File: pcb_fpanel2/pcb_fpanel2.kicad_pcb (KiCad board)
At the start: 2 copper layers, 155.5 x 65.5 mm, 22 parts, among them J1 Conn_01x10, SW1 SW_Push_LED, SW2 SW_Push_LED, SW3 SW_Push_LED, SW4 SW_Push_LED, SW5 SW_Push_LED, SW6 SW_Push_LED, SW7 SW_Push_LED, SW8 SW_Push_LED, SW9 SW_Push_LED

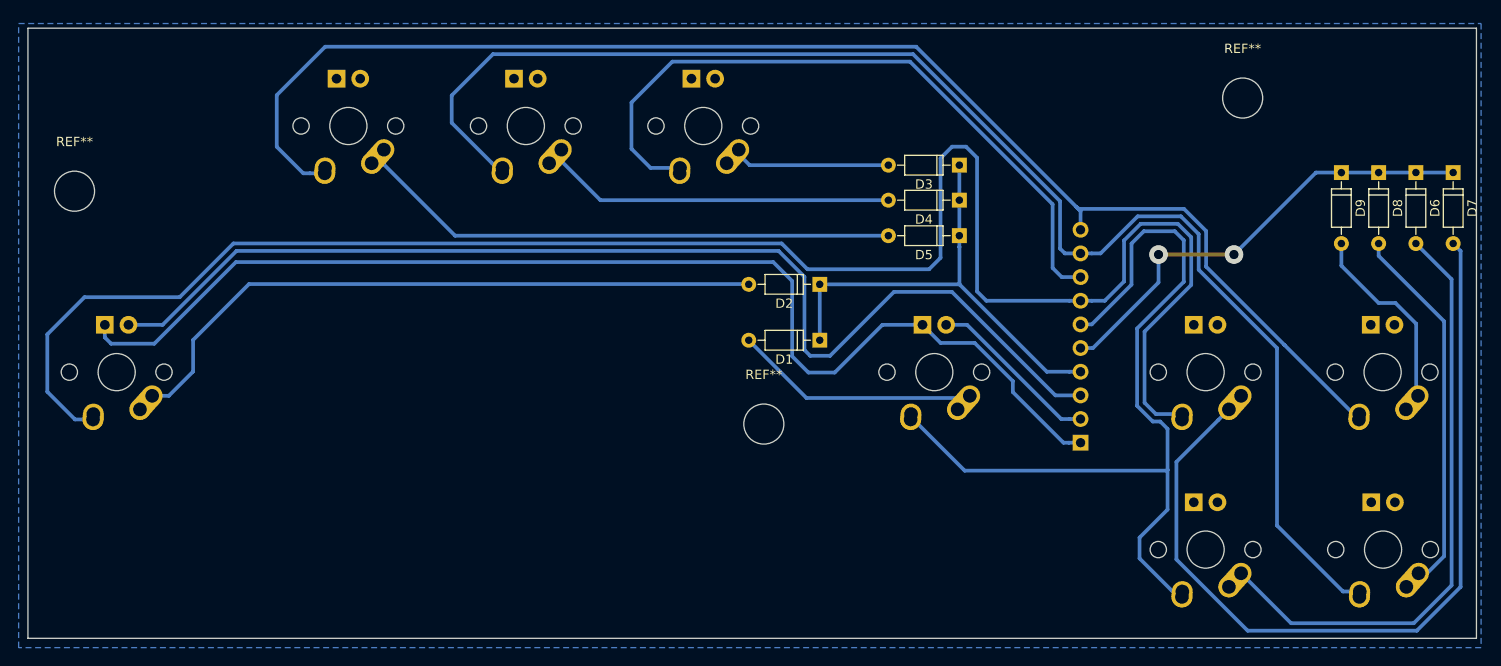
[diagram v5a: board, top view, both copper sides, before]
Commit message: Näppäinten sijainnit ja footprintit päivitetty
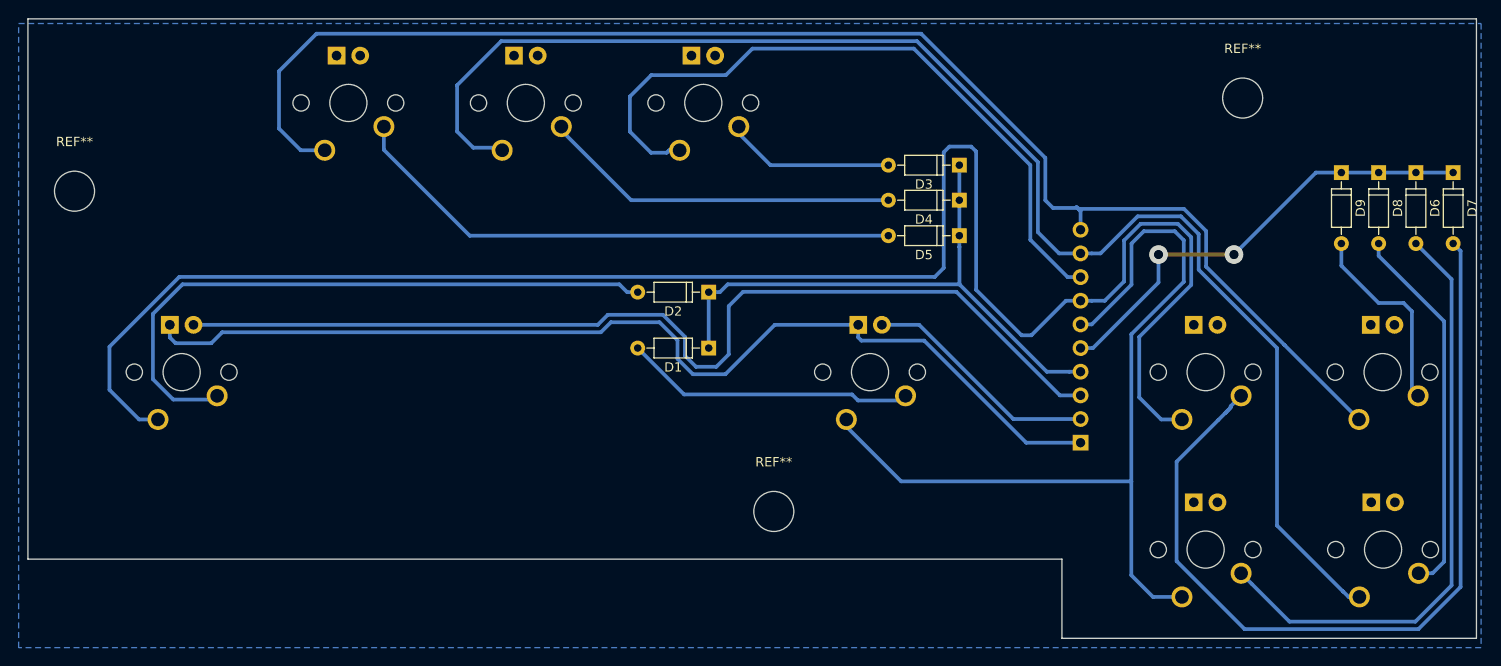
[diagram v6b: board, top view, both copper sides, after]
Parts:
- SW1, SW2, SW3, SW4, SW5, SW6, SW7, SW8, SW9: footprint MX_Alps_Hybrid:MX-1U -> MX_Only:MXOnly-1U
- moved D1 11.9 mm to (102.1, 135.8)
- moved D2 11.9 mm to (102.1, 129.8)
- moved REF** 9.44 mm to (109.1, 153.4)
- moved SW2 6.98 mm to (45.5, 138.4)
- moved SW1 6.90 mm to (119.4, 138.4)
- moved SW3 2.47 mm to (101.5, 109.5)
- moved SW4 2.47 mm to (82.5, 109.5)
- moved SW5 2.47 mm to (63.4, 109.5)
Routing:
- net GNDD: track 127.7 -> 112.0 mm
- net row_1: track 50.7 -> 63.0 mm
- net led_1: track 122.2 -> 110.2 mm
- net led_2: track 18.6 -> 25.5 mm
- net Net-(D1-Pad2): track 26.4 -> 31.3 mm
- net column_2: track 198.5 -> 194.0 mm
- net column_1: track 93.8 -> 97.3 mm
- net column_4: track 151.6 -> 154.7 mm
- net Net-(D7-Pad2): track 91.3 -> 93.7 mm
- net Net-(D2-Pad2): track 71.0 -> 68.7 mm
- net column_3: track 153.5 -> 155.3 mm
- net Net-(D5-Pad2): track 58.9 -> 60.5 mm
- net Net-(D3-Pad2): track 17.0 -> 18.2 mm
- net column_5: track 74.6 -> 75.5 mm
- net Net-(D4-Pad2): track 38.1 -> 38.6 mm
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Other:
- board size 155.5 x 65.5 mm -> 155.5 x 66.5 mm
